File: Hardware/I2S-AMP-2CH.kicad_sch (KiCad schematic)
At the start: 19 parts, among them U7 TAS5760MDCAR

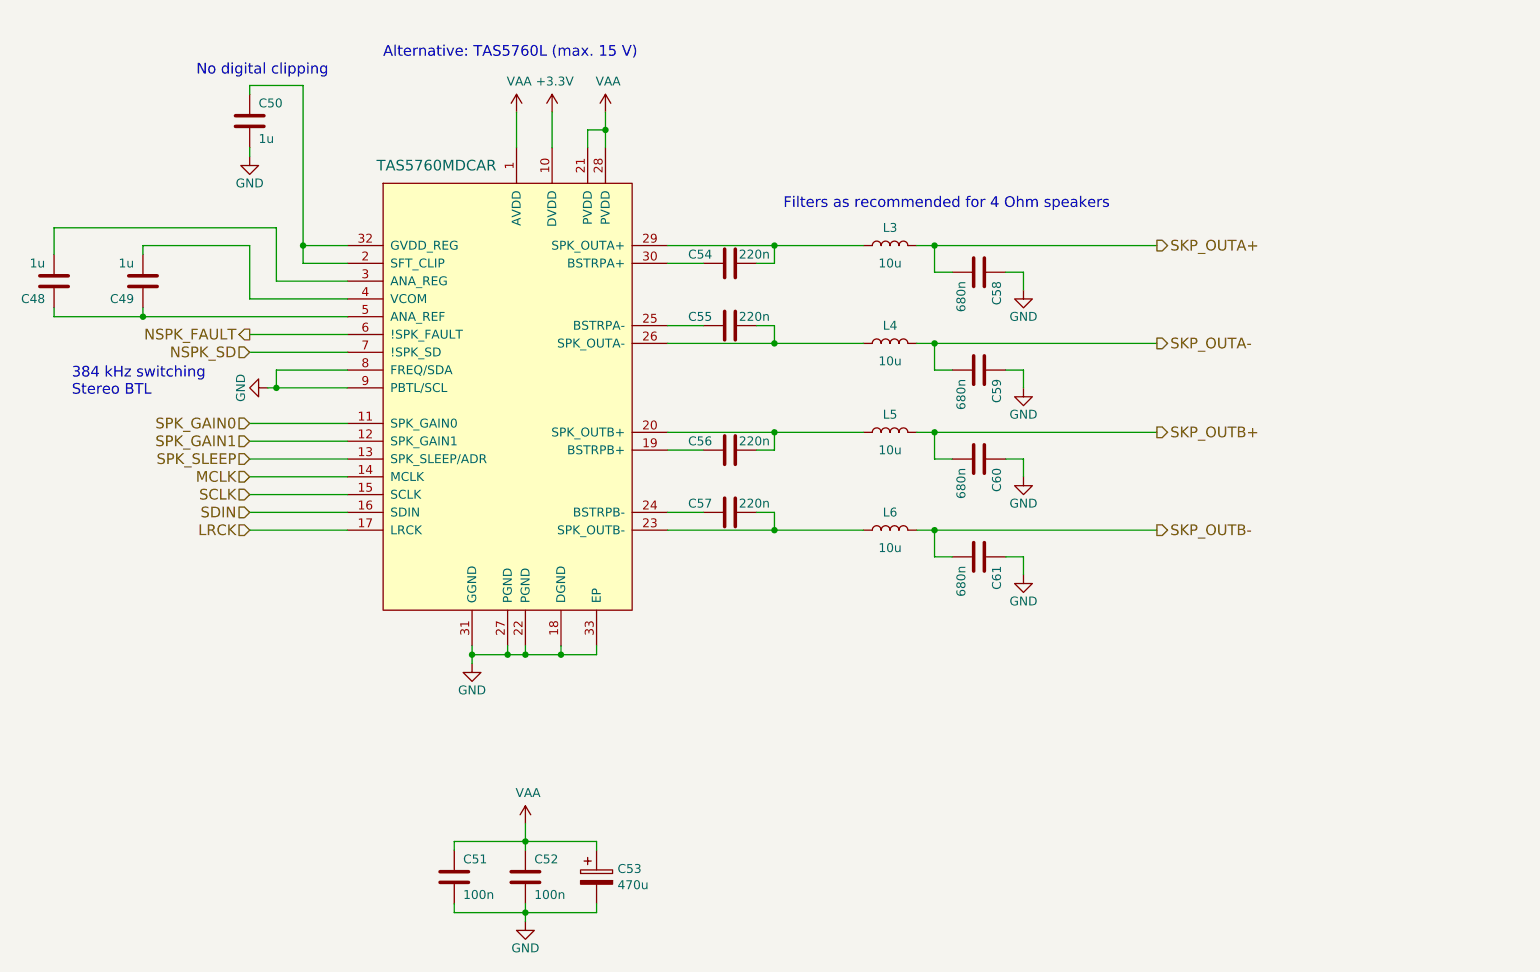
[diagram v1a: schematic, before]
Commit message: Updated clock buffer
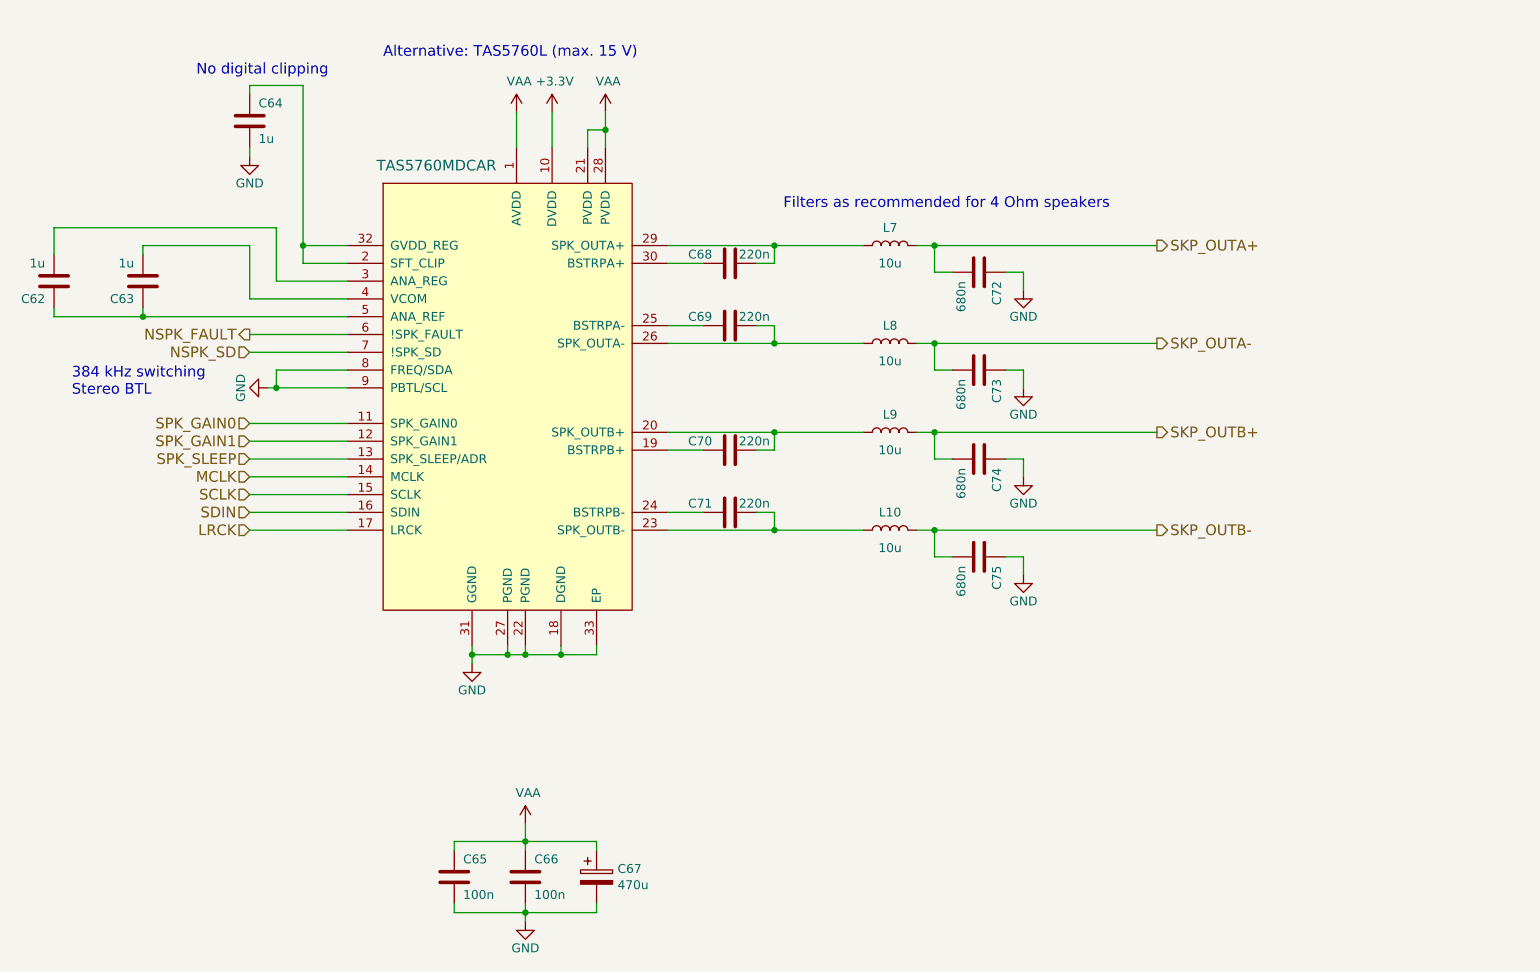
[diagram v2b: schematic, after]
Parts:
- renumbered C48 to C62, C49 to C63, C50 to C64, C51 to C65, C52 to C66, C53 to C67, C54 to C68, C55 to C69, C56 to C70, C57 to C71, C58 to C72, C59 to C73, C60 to C74, C61 to C75, L6 to L10, L3 to L7, L4 to L8, L5 to L9, U7 to U8
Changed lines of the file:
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@@
   (symbol (lib_id "Device:C") (at 74.93 41.91 0)
     (in_bom yes) (on_board yes)
-    (property "Reference" "C50" (id 0) (at 76.2 39.37 0)
+    (property "Reference" "C64" (id 0) (at 76.2 39.37 0)
       (effects (font (size 1.27 1.27)) (justify left))
     )
@@
   (symbol (lib_id "Device:C") (at 114.3 149.86 0)
     (in_bom yes) (on_board yes)
-    (property "Reference" "C52" (id 0) (at 115.57 147.32 0)
+    (property "Reference" "C66" (id 0) (at 115.57 147.32 0)
       (effects (font (size 1.27 1.27)) (justify left))
     )
@@
   (symbol (lib_id "Device:C") (at 59.69 64.77 180)
     (in_bom yes) (on_board yes)
-    (property "Reference" "C49" (id 0) (at 58.42 67.31 0)
+    (property "Reference" "C63" (id 0) (at 58.42 67.31 0)
       (effects (font (size 1.27 1.27)) (justify left))
     )
@@
   (symbol (lib_id "Device:C") (at 46.99 64.77 180)
     (in_bom yes) (on_board yes)
-    (property "Reference" "C48" (id 0) (at 45.72 67.31 0)
+    (property "Reference" "C62" (id 0) (at 45.72 67.31 0)
       (effects (font (size 1.27 1.27)) (justify left))
     )
@@
   (symbol (lib_id "power:GND") (at 114.3 156.21 0)
     (in_bom yes) (on_board yes)
-    (property "Reference" "#PWR068" (id 0) (at 114.3 162.56 0)
+    (property "Reference" "#PWR080" (id 0) (at 114.3 162.56 0)
       (effects (font (size 1.27 1.27)) hide)
     )
@@
   (symbol (lib_id "power:GND") (at 74.93 46.99 0)
     (in_bom yes) (on_board yes)
-    (property "Reference" "#PWR063" (id 0) (at 74.93 53.34 0)
+    (property "Reference" "#PWR075" (id 0) (at 74.93 53.34 0)
       (effects (font (size 1.27 1.27)) hide)
     )
@@
   (symbol (lib_id "Device:C") (at 143.51 97.79 90)
     (in_bom yes) (on_board yes)
-    (property "Reference" "C57" (id 0) (at 140.97 96.52 90)
+    (property "Reference" "C71" (id 0) (at 140.97 96.52 90)
       (effects (font (size 1.27 1.27)) (justify left))
     )
@@
   (symbol (lib_id "Device:C") (at 143.51 71.12 90)
     (in_bom yes) (on_board yes)
-    (property "Reference" "C55" (id 0) (at 140.97 69.85 90)
+    (property "Reference" "C69" (id 0) (at 140.97 69.85 90)
       (effects (font (size 1.27 1.27)) (justify left))
     )
@@
   (symbol (lib_id "Device:C") (at 143.51 62.23 90)
     (in_bom yes) (on_board yes)
-    (property "Reference" "C54" (id 0) (at 140.97 60.96 90)
+    (property "Reference" "C68" (id 0) (at 140.97 60.96 90)
       (effects (font (size 1.27 1.27)) (justify left))
     )
@@
   (symbol (lib_id "Device:L") (at 166.37 59.69 90)
     (in_bom yes) (on_board yes)
-    (property "Reference" "L3" (id 0) (at 166.37 57.15 90))
+    (property "Reference" "L7" (id 0) (at 166.37 57.15 90))
     (property "Value" "10u" (id 1) (at 166.37 62.23 90))
     (property "Footprint" "Inductor_SMD:L_Abracon_ASPI-0630LR" (id 2) (at 166.37 59.69 0)
@@
   (symbol (lib_id "Device:C") (at 179.07 63.5 270)
     (in_bom yes) (on_board yes)
-    (property "Reference" "C58" (id 0) (at 181.61 64.77 0)
+    (property "Reference" "C72" (id 0) (at 181.61 64.77 0)
       (effects (font (size 1.27 1.27)) (justify left))
     )
@@
   (symbol (lib_id "power:VAA") (at 114.3 142.24 0)
     (in_bom yes) (on_board yes)
-    (property "Reference" "#PWR067" (id 0) (at 114.3 146.05 0)
+    (property "Reference" "#PWR079" (id 0) (at 114.3 146.05 0)
       (effects (font (size 1.27 1.27)) hide)
     )
@@
   (symbol (lib_id "tas5760:TAS5760MDCAR") (at 111.76 81.28 0)
     (in_bom yes) (on_board yes)
-    (property "Reference" "U7" (id 0) (at 111.76 31.75 0)
+    (property "Reference" "U8" (id 0) (at 111.76 31.75 0)
       (effects (font (size 1.524 1.524)) (justify top) hide)
     )
@@
   (symbol (lib_id "power:+3.3V") (at 118.11 40.64 0)
     (in_bom yes) (on_board yes)
-    (property "Reference" "#PWR069" (id 0) (at 118.11 44.45 0)
+    (property "Reference" "#PWR081" (id 0) (at 118.11 44.45 0)
       (effects (font (size 1.27 1.27)) hide)
     )
@@
   (symbol (lib_id "power:VAA") (at 125.73 40.64 0)
     (in_bom yes) (on_board yes)
-    (property "Reference" "#PWR070" (id 0) (at 125.73 44.45 0)
+    (property "Reference" "#PWR082" (id 0) (at 125.73 44.45 0)
       (effects (font (size 1.27 1.27)) hide)
     )
@@
   (symbol (lib_id "power:VAA") (at 113.03 40.64 0)
     (in_bom yes) (on_board yes)
-    (property "Reference" "#PWR066" (id 0) (at 113.03 44.45 0)
+    (property "Reference" "#PWR078" (id 0) (at 113.03 44.45 0)
       (effects (font (size 1.27 1.27)) hide)
     )
@@
   (symbol (lib_id "power:GND") (at 106.68 119.38 0)
     (in_bom yes) (on_board yes)
-    (property "Reference" "#PWR065" (id 0) (at 106.68 125.73 0)
+    (property "Reference" "#PWR077" (id 0) (at 106.68 125.73 0)
       (effects (font (size 1.27 1.27)) hide)
     )
@@
   (symbol (lib_id "Device:CP") (at 124.46 149.86 0)
     (in_bom yes) (on_board yes)
-    (property "Reference" "C53" (id 0) (at 127.4572 148.6916 0)
+    (property "Reference" "C67" (id 0) (at 127.4572 148.6916 0)
       (effects (font (size 1.27 1.27)) (justify left))
     )
@@
   (symbol (lib_id "Device:C") (at 104.14 149.86 0)
     (in_bom yes) (on_board yes)
-    (property "Reference" "C51" (id 0) (at 105.41 147.32 0)
+    (property "Reference" "C65" (id 0) (at 105.41 147.32 0)
       (effects (font (size 1.27 1.27)) (justify left))
     )
@@
   (symbol (lib_id "power:GND") (at 77.47 80.01 270)
     (in_bom yes) (on_board yes)
-    (property "Reference" "#PWR064" (id 0) (at 71.12 80.01 0)
+    (property "Reference" "#PWR076" (id 0) (at 71.12 80.01 0)
       (effects (font (size 1.27 1.27)) hide)
     )
@@
   (symbol (lib_id "Device:C") (at 143.51 88.9 90)
     (in_bom yes) (on_board yes)
-    (property "Reference" "C56" (id 0) (at 140.97 87.63 90)
+    (property "Reference" "C70" (id 0) (at 140.97 87.63 90)
       (effects (font (size 1.27 1.27)) (justify left))
     )
@@
   (symbol (lib_id "Device:L") (at 166.37 73.66 90)
     (in_bom yes) (on_board yes)
-    (property "Reference" "L4" (id 0) (at 166.37 71.12 90))
+    (property "Reference" "L8" (id 0) (at 166.37 71.12 90))
     (property "Value" "10u" (id 1) (at 166.37 76.2 90))
     (property "Footprint" "Inductor_SMD:L_Abracon_ASPI-0630LR" (id 2) (at 166.37 73.66 0)
@@
   (symbol (lib_id "Device:L") (at 166.37 86.36 90)
     (in_bom yes) (on_board yes)
-    (property "Reference" "L5" (id 0) (at 166.37 83.82 90))
+    (property "Reference" "L9" (id 0) (at 166.37 83.82 90))
     (property "Value" "10u" (id 1) (at 166.37 88.9 90))
     (property "Footprint" "Inductor_SMD:L_Abracon_ASPI-0630LR" (id 2) (at 166.37 86.36 0)
@@
   (symbol (lib_id "Device:L") (at 166.37 100.33 90)
     (in_bom yes) (on_board yes)
-    (property "Reference" "L6" (id 0) (at 166.37 97.79 90))
+    (property "Reference" "L10" (id 0) (at 166.37 97.79 90))
     (property "Value" "10u" (id 1) (at 166.37 102.87 90))
     (property "Footprint" "Inductor_SMD:L_Abracon_ASPI-0630LR" (id 2) (at 166.37 100.33 0)
@@
   (symbol (lib_id "Device:C") (at 179.07 77.47 270)
     (in_bom yes) (on_board yes)
-    (property "Reference" "C59" (id 0) (at 181.61 78.74 0)
+    (property "Reference" "C73" (id 0) (at 181.61 78.74 0)
       (effects (font (size 1.27 1.27)) (justify left))
     )
@@
   (symbol (lib_id "Device:C") (at 179.07 90.17 270)
     (in_bom yes) (on_board yes)
-    (property "Reference" "C60" (id 0) (at 181.61 91.44 0)
+    (property "Reference" "C74" (id 0) (at 181.61 91.44 0)
       (effects (font (size 1.27 1.27)) (justify left))
     )
@@
   (symbol (lib_id "Device:C") (at 179.07 104.14 270)
     (in_bom yes) (on_board yes)
-    (property "Reference" "C61" (id 0) (at 181.61 105.41 0)
+    (property "Reference" "C75" (id 0) (at 181.61 105.41 0)
       (effects (font (size 1.27 1.27)) (justify left))
     )
@@
   (symbol (lib_id "power:GND") (at 185.42 66.04 0)
     (in_bom yes) (on_board yes)
-    (property "Reference" "#PWR071" (id 0) (at 185.42 72.39 0)
+    (property "Reference" "#PWR083" (id 0) (at 185.42 72.39 0)
       (effects (font (size 1.27 1.27)) hide)
     )
@@
   (symbol (lib_id "power:GND") (at 185.42 80.01 0)
     (in_bom yes) (on_board yes)
-    (property "Reference" "#PWR072" (id 0) (at 185.42 86.36 0)
+    (property "Reference" "#PWR084" (id 0) (at 185.42 86.36 0)
       (effects (font (size 1.27 1.27)) hide)
     )
@@
   (symbol (lib_id "power:GND") (at 185.42 92.71 0)
     (in_bom yes) (on_board yes)
-    (property "Reference" "#PWR073" (id 0) (at 185.42 99.06 0)
+    (property "Reference" "#PWR085" (id 0) (at 185.42 99.06 0)
       (effects (font (size 1.27 1.27)) hide)
     )
@@
   (symbol (lib_id "power:GND") (at 185.42 106.68 0)
     (in_bom yes) (on_board yes)
-    (property "Reference" "#PWR074" (id 0) (at 185.42 113.03 0)
-      (effects (font (size 1.27 1.27)) hide)
-    )
+    (property "Reference" "#PWR086" (id 0) (at 185.42 113.03 0)
+      (effects (font (size 1.27 1.27)) hide)
+    )

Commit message: feat: updated amplifier IC, finalized design
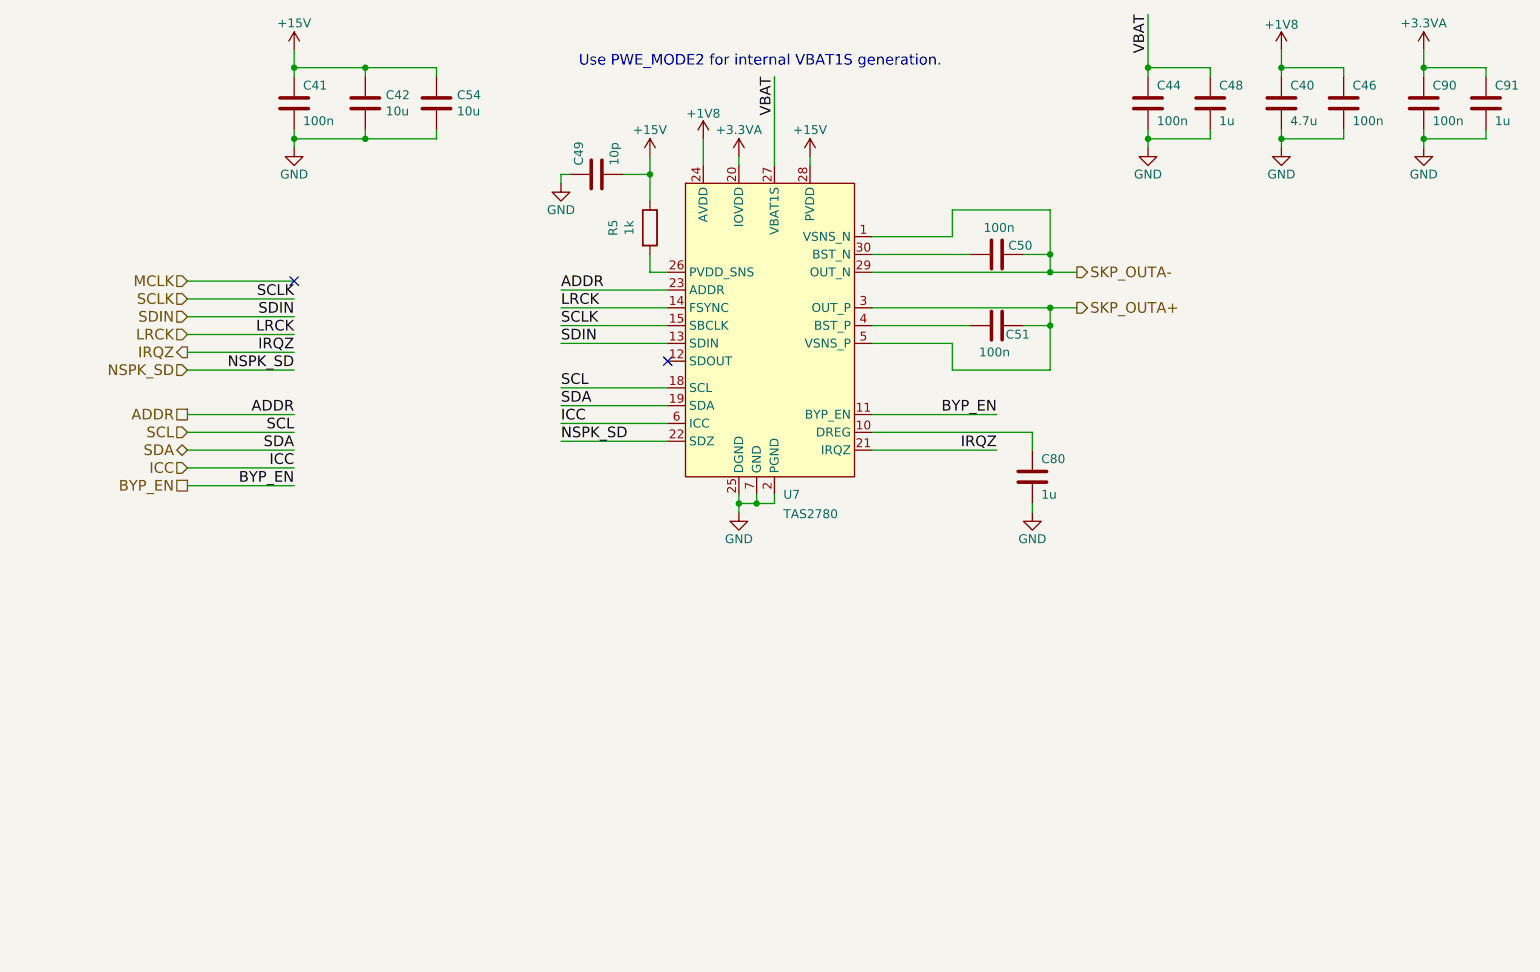
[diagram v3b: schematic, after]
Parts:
- removed C62, C63, C64: 1u, Capacitor_SMD:C_0805_2012Metric_Pad1.18x1.45mm_HandSolder, symbol Device:C
- removed C65: 100n, Capacitor_SMD:C_0603_1608Metric_Pad1.08x0.95mm_HandSolder, symbol Device:C
- removed C67: 470u, Capacitor_THT:CP_Radial_D16.0mm_P7.50mm, symbol Device:CP
- removed C68, C69, C70, C71: 220n, Capacitor_SMD:C_0603_1608Metric_Pad1.08x0.95mm_HandSolder, symbol Device:C
- removed C72, C73, C74, C75: 680n, Capacitor_SMD:C_0805_2012Metric_Pad1.18x1.45mm_HandSolder, symbol Device:C
- removed L10, L7, L8, L9: 10u, Inductor_SMD:L_Abracon_ASPI-0630LR, symbol Device:L
- removed U8: TAS5760MDCAR, Package_SO:HTSSOP-32-1EP_6.1x11mm_P0.65mm_EP5.2x11mm_Mask4.11x4.36mm_ThermalVias, symbol tas5760:TAS5760MDCAR
- added C40: 4.7u, Capacitor_SMD:C_0805_2012Metric, symbol Device:C
- added C42, C54: 10u, Capacitor_SMD:C_1206_3216Metric, symbol Device:C
- added C44, C46, C50, C51, C90: 100n, Capacitor_SMD:C_0402_1005Metric, symbol Device:C
- added C48, C80, C91: 1u, Capacitor_SMD:C_0603_1608Metric, symbol Device:C
- added C49: 10p, Capacitor_SMD:C_0402_1005Metric, symbol Device:C
- added R5: 1k, Resistor_SMD:R_0402_1005Metric, symbol Device:R
- added U7: TAS2780, TI-QFN:TI-30-Pin-HR-QFN, symbol tas2820:TAS2780
- C41: renamed from C66; footprint Capacitor_SMD:C_0603_1608Metric_Pad1.08x0.95mm_HandSolder -> Capacitor_SMD:C_0402_1005Metric
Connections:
- net GND: now also C40.2, C42.2, C44.2, C46.2, C48.2, C49.1, C54.2, C80.2, C90.2, C91.2, U7.2 (PGND), U7.25 (DGND), U7.7 (GND)
- net LRCK: now also U7.14 (FSYNC)
- net NSPK_SD: now also U7.22 (SDZ)
- net SCLK: now also U7.15 (SBCLK)
- net SDIN: now also U7.13 (SDIN)
- net SKP_OUTA+: now also C51.1, U7.3 (OUT_P), U7.5 (VSNS_P)
- net SKP_OUTA-: now also C50.2, U7.1 (VSNS_N), U7.29 (OUT_N)
- net VAA renamed +15V
- net +15V: now also C42.1, C49.2, C54.1, R5.1, U7.28 (PVDD)
- new net: C80.1, U7.10 (DREG)
- new net: R5.2, U7.26 (PVDD_SNS)
- new net: C50.1, U7.30 (BST_N)
- new net: C51.2, U7.4 (BST_P)
- new net +1V8: C40.1, C46.1, U7.24 (AVDD)
- new net +3.3VA: C90.1, C91.1, U7.20 (IOVDD)
- new net ADDR: U7.23 (ADDR)
- new net BYP_EN: U7.11 (BYP_EN)
- new net ICC: U7.6 (ICC)
- new net IRQZ: U7.21 (IRQZ)
- new net SCL: U7.18 (SCL)
- new net SDA: U7.19 (SDA)
- new net VBAT: C44.1, C48.1, U7.27 (VBAT1S)
- no-connect marks 0 -> 2
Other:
- note added: "Use PWE_MODE2 for internal VBAT1S generation."
- note removed: "384 kHz switching Stereo BTL"
- note removed: "Alternative: TAS5760L (max. 15 V)"
- note removed: "Filters as recommended for 4 Ohm speakers"
- note removed: "No digital clipping"
- moved on the sheet: C41

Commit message: prod. version blus mini a
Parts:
- C15: renamed from C80; MPN (none) -> C15849; Mfr.Nr. GRM188R71H104KA93D -> (none)
- C16: renamed from C42; MPN (none) -> C13585
- C23: renamed from C41; MPN (none) -> C307331; Mfr.Nr. GRM188R71H104KA93D -> (none)
- C24: renamed from C49; MPN (none) -> C32949; Mfr.Nr. GRM188R71H104KA93D -> (none)
- C28: renamed from C44; MPN (none) -> C307331; Mfr.Nr. GRM188R71H104KA93D -> (none)
- C32: renamed from C48; MPN (none) -> C15849; Mfr.Nr. GRM188R71H104KA93D -> (none)
- C39: renamed from C46; MPN (none) -> C307331; Mfr.Nr. GRM188R71H104KA93D -> (none)
- C40: renamed from C54; MPN (none) -> C13585
- C44: renamed from C90; MPN (none) -> C307331; Mfr.Nr. GRM188R71H104KA93D -> (none)
- C51: renamed from C91; MPN (none) -> C15849; Mfr.Nr. GRM188R71H104KA93D -> (none)
- C52: renamed from C40; MPN (none) -> C1779; Mfr.Nr. GRM31CR71H475KA12L -> (none)
- C7: renamed from C51; MPN (none) -> C307331; Mfr.Nr. GRM188R71H104KA93D -> (none)
- C8: renamed from C50; MPN (none) -> C307331; Mfr.Nr. GRM188R71H104KA93D -> (none)
- R4: renamed from R5; MPN (none) -> C11702
- renumbered U7 to U4
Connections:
- net +15V renamed VPP
- net +3.3VA renamed +3.3V
- net BYP_EN: no longer names the net of U4.11 (BYP_EN)

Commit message: feat!: wip, version b
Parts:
- U4: footprint TI-QFN:TI-30-Pin-HR-QFN -> Package_TI_QFN:TI-30-Pin-HR-QFN; symbol tas2820:TAS2780 -> Amplifiers_Audio_Switching:TAS2780; Mfr.Nr. (none) -> M
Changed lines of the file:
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@@
     (pin "1")
   )
-  (symbol (lib_id "tas2820:TAS2780") (at 148.59 52.07 0) (unit 1)
+  (symbol (lib_id "Amplifiers_Audio_Switching:TAS2780") (at 148.59 52.07 0) (unit 1)
     (in_bom yes) (on_board yes)
     (property "Reference" "U4" (id 0) (at 151.13 95.25 0)
@@
       (effects (font (size 1.27 1.27)) (justify left))
     )
-    (property "Footprint" "TI-QFN:TI-30-Pin-HR-QFN" (id 2) (at 158.75 48.26 0)
+    (property "Footprint" "Package_TI_QFN:TI-30-Pin-HR-QFN" (id 2) (at 158.75 48.26 0)
       (effects (font (size 1.27 1.27)) hide)
     )
@@
       (effects (font (size 1.27 1.27)) hide)
     )
-    (property "Mfr.Nr." "" (id 4) (at 148.59 52.07 0)
+    (property "Mfr.Nr." "M" (id 4) (at 148.59 52.07 0)
       (effects (font (size 1.27 1.27)) hide)
     )
